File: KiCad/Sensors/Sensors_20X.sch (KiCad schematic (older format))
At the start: 17 parts, among them J1 Conn_02x06_Odd_Even, U1 OPA1641

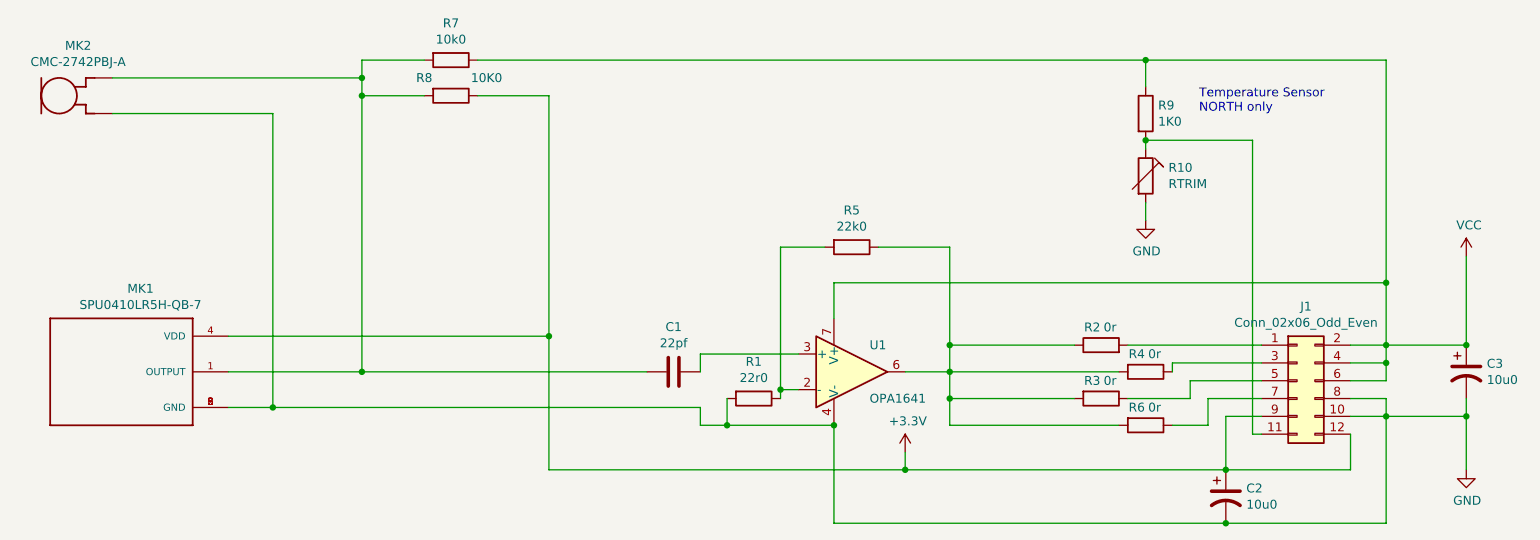
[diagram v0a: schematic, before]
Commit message: Pushing Sensor Revisions
Sensors revised for inverting signal.

Needed since the 'bang' is a negative going wave form that needs to be inverted
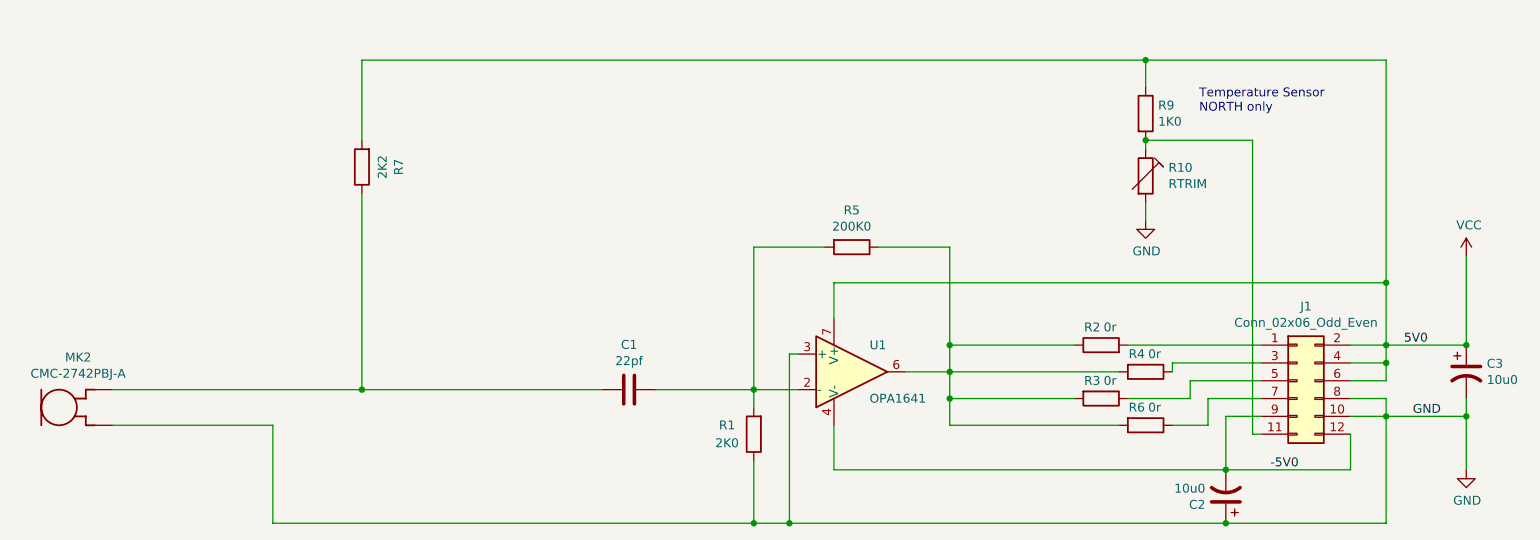
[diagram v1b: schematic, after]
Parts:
- removed MK1: SPU0410LR5H-QB-7, SnapEDA:MIC_SPU0410LR5H-QB-7, symbol SPU0410LR5H-QB-7:SPU0410LR5H-QB-7
- removed R8: 10K0, Resistor_SMD:R_0805_2012Metric, symbol Device:R
- R1: value 22r0 -> 2K0
- R5: value 22k0 -> 200K0
- R7: value 10k0 -> 2K2
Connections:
- net GND: now also C2.1, R1.1, U1.3 (+); no longer C2.2, R1.2, U1.4 (V-)
- net VCC: now also R7.2; no longer R7.1
- net at C1.2, MK2.OUT: now also R7.1; no longer R7.2
- net at R5.2, U1.2 (-): now also C1.1, R1.2; no longer R1.1
- net +3V3 renamed -5V0
- net -5V0: now also C2.2, U1.4 (V-); no longer C2.1
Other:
- moved on the sheet: C1, MK2, R1, R7
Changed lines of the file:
@@
 encoding utf-8
 Sheet 1 1
-Title ""
-Date ""
-Rev ""
+Title "freETarget Sensor Module"
+Date "April 4, 2020"
+Rev "1.0.X"
 Comp ""
-Comment1 ""
+Comment1 "General purpose version for sensor development"
 Comment2 ""
 Comment3 ""
 Comment4 ""
 $EndDescr
-$Comp
-L SPU0410LR5H-QB-7:SPU0410LR5H-QB-7 MK1
-U 1 1 5E68DAEF
-P 2600 4000
-F 0 "MK1" H 2707 4467 50  0000 C CNN
-F 1 "SPU0410LR5H-QB-7" H 2707 4376 50  0000 C CNN
-F 2 "SnapEDA:MIC_SPU0410LR5H-QB-7" H 2600 4000 50  0001 L BNN
-F 3 "Knowles" H 2600 4000 50  0001 L BNN
-F 4 "Manufacturer Recommendations" H 2600 4000 50  0001 L BNN "Field4"
-F 5 "1.2mm" H 2600 4000 50  0001 L BNN "Field5"
-F 6 "H" H 2600 4000 50  0001 L BNN "Field6"
-	1    2600 4000
-	1    0    0    -1
-$EndComp
 $Comp
 L Amplifier_Operational:OPA1641 U1
@@
 $EndComp
 Wire Wire Line
-	6600 4300 6000 4300
-Wire Wire Line
 	7000 4000 7250 4000
 $Comp
 L Device:C C1
 U 1 1 5E6A1DD7
-P 5700 4000
-F 0 "C1" V 5448 4000 50  0000 C CNN
-F 1 "22pf" V 5539 4000 50  0000 C CNN
-F 2 "Resistor_SMD:R_0805_2012Metric" H 5738 3850 50  0001 C CNN
-F 3 "~" H 5700 4000 50  0001 C CNN
-	1    5700 4000
+P 5450 4100
+F 0 "C1" V 5198 4100 50  0000 C CNN
+F 1 "22pf" V 5289 4100 50  0000 C CNN
+F 2 "Resistor_SMD:R_0805_2012Metric" H 5488 3950 50  0001 C CNN
+F 3 "~" H 5450 4100 50  0001 C CNN
+	1    5450 4100
 	0    1    1    0
 $EndComp
@@
 P 6700 3300
 F 0 "R5" V 6493 3300 50  0000 C CNN
-F 1 "22k0" V 6584 3300 50  0000 C CNN
+F 1 "200K0" V 6584 3300 50  0000 C CNN
 F 2 "Resistor_SMD:R_0805_2012Metric" V 6630 3300 50  0001 C CNN
 F 3 "~" H 6700 3300 50  0001 C CNN
@@
 L Device:R R1
 U 1 1 5E6A320A
-P 6150 4150
-F 0 "R1" V 5943 4150 50  0000 C CNN
-F 1 "22r0" V 6034 4150 50  0000 C CNN
-F 2 "Resistor_SMD:R_0805_2012Metric" V 6080 4150 50  0001 C CNN
-F 3 "~" H 6150 4150 50  0001 C CNN
-	1    6150 4150
-	0    1    1    0
-$EndComp
-Wire Wire Line
-	6400 3900 5850 3900
-Wire Wire Line
-	5850 3900 5850 4000
+P 6150 4350
+F 0 "R1" H 6300 4300 50  0000 C CNN
+F 1 "2K0" H 6300 4400 50  0000 C CNN
+F 2 "Resistor_SMD:R_0805_2012Metric" V 6080 4350 50  0001 C CNN
+F 3 "~" H 6150 4350 50  0001 C CNN
+	1    6150 4350
+	-1   0    0    1
+$EndComp
 Wire Wire Line
 	7250 4000 7250 3850
@@
 	7250 3300 6850 3300
 Wire Wire Line
-	6550 3300 6300 3300
-Wire Wire Line
-	6300 3300 6300 4100
-Wire Wire Line
-	6400 4100 6300 4100
-Connection ~ 6300 4100
-Wire Wire Line
-	6300 4100 6300 4150
-Wire Wire Line
-	6000 4150 6000 4300
-Connection ~ 6000 4300
+	6150 3300 6150 4100
 $Comp
 L Device:R R4
@@
 Wire Wire Line
 	9700 4150 9500 4150
-Connection ~ 6600 4300
 Wire Wire Line
 	9500 4250 9700 4250
@@
 F 3 "~" H 8800 4700 50  0001 C CNN
 	1    8800 4700
-	1    0    0    -1
+	-1   0    0    1
 $EndComp
 Wire Wire Line
 	9700 4250 9700 4850
-Wire Wire Line
-	8800 4850 6600 4850
-Wire Wire Line
-	6600 4300 6600 4850
-Connection ~ 8800 4850
 Wire Wire Line
 	10150 4250 9700 4250
@@
 	10150 3850 9700 3850
 Connection ~ 9700 3500
-Wire Wire Line
-	3200 4200 3450 4200
 $Comp
 L Device:R R7
 U 1 1 5E7A9A5C
-P 4450 2250
-F 0 "R7" V 4243 2250 50  0000 C CNN
-F 1 "10k0" V 4334 2250 50  0000 C CNN
-F 2 "Resistor_SMD:R_0805_2012Metric" V 4380 2250 50  0001 C CNN
-F 3 "~" H 4450 2250 50  0001 C CNN
-	1    4450 2250
-	0    1    1    0
+P 3950 2850
+F 0 "R7" V 3743 2850 50  0000 C CNN
+F 1 "2K2" V 3834 2850 50  0000 C CNN
+F 2 "Resistor_SMD:R_0805_2012Metric" V 3880 2850 50  0001 C CNN
+F 3 "~" H 3950 2850 50  0001 C CNN
+	1    3950 2850
+	-1   0    0    1
 $EndComp
 Wire Wire Line
 	9700 2250 9700 3500
-Wire Wire Line
-	4300 2450 3950 2450
-Wire Wire Line
-	3200 4000 3950 4000
-Connection ~ 3450 4200
-Wire Wire Line
-	3950 2450 3950 4000
-Connection ~ 3950 2450
-Connection ~ 3950 4000
-Wire Wire Line
-	3950 4000 5550 4000
-Wire Wire Line
-	5000 2450 5000 3800
-Wire Wire Line
-	3200 3800 5000 3800
-Wire Wire Line
-	4600 2450 5000 2450
-Wire Wire Line
-	4600 2250 8350 2250
-Wire Wire Line
-	5850 4300 5850 4200
-Wire Wire Line
-	3450 4200 5850 4200
-Wire Wire Line
-	5850 4300 6000 4300
-$Comp
-L Device:R R8
-U 1 1 5E7AA2E7
-P 4450 2450
-F 0 "R8" V 4350 2300 50  0000 C CNN
-F 1 "10K0" V 4350 2650 50  0000 C CNN
-F 2 "Resistor_SMD:R_0805_2012Metric" V 4380 2450 50  0001 C CNN
-F 3 "~" H 4450 2450 50  0001 C CNN
-	1    4450 2450
-	0    1    1    0
-$EndComp
-Wire Wire Line
-	3950 2250 4300 2250
 $Comp
 L power:GND #PWR0101
@@
 	10150 4150 10150 4250
 $Comp
-L power:+3.3V #PWR0103
-U 1 1 5E81B6EE
-P 7000 4450
-F 0 "#PWR0103" H 7000 4300 50  0001 C CNN
-F 1 "+3.3V" H 7015 4623 50  0000 C CNN
-F 2 "" H 7000 4450 50  0001 C CNN
-F 3 "" H 7000 4450 50  0001 C CNN
-	1    7000 4450
-	1    0    0    -1
-$EndComp
-Wire Wire Line
-	7000 4450 7000 4550
-Wire Wire Line
-	3450 2550 3450 4200
-$Comp
 L CMC-2742PBJ-A:CMC-2742PBJ-A MK2
 U 1 1 5E7C8206
-P 2250 2450
-F 0 "MK2" H 2357 2731 50  0000 C CNN
-F 1 "CMC-2742PBJ-A" H 2357 2640 50  0000 C CNN
-F 2 "CUI_CMC-2742PBJ-A" H 2250 2450 50  0001 L BNN
-F 3 "CUI INC" H 2250 2450 50  0001 L BNN
-F 4 "Manufacturer recommendations" H 2250 2450 50  0001 L BNN "Field4"
-	1    2250 2450
+P 2250 4200
+F 0 "MK2" H 2357 4481 50  0000 C CNN
+F 1 "CMC-2742PBJ-A" H 2357 4390 50  0000 C CNN
+F 2 "CUI_CMC-2742PBJ-A" H 2250 4200 50  0001 L BNN
+F 3 "CUI INC" H 2250 4200 50  0001 L BNN
+F 4 "Manufacturer recommendations" H 2250 4200 50  0001 L BNN "Field4"
+	1    2250 4200
 	1    0    0    -1
 $EndComp
@@
 $EndComp
 Wire Wire Line
-	7000 4550 8800 4550
-Wire Wire Line
 	8800 4550 9500 4550
-Wire Wire Line
-	8800 4850 9700 4850
 Wire Wire Line
 	9000 4250 8800 4250
@@
 Temperature Sensor\nNORTH only
 Wire Wire Line
-	3950 2250 3950 2350
-Wire Wire Line
-	2550 2550 3450 2550
-Wire Wire Line
-	2550 2350 3950 2350
-Connection ~ 3950 2350
-Wire Wire Line
-	3950 2350 3950 2450
-Wire Wire Line
-	7000 4550 5000 4550
-Wire Wire Line
-	5000 4550 5000 3800
-Connection ~ 7000 4550
-Connection ~ 5000 3800
+	2550 4300 3450 4300
+Wire Wire Line
+	8800 4850 9700 4850
+Wire Wire Line
+	8800 4550 6600 4550
+Wire Wire Line
+	6600 4550 6600 4300
+Text Label 9050 4550 0    50   ~ 0
+-5V0
+Connection ~ 6150 4100
+Wire Wire Line
+	6150 4200 6150 4100
+Wire Wire Line
+	6150 4500 6150 4850
+Wire Wire Line
+	5600 4100 6150 4100
+Wire Wire Line
+	6150 4100 6400 4100
+Wire Wire Line
+	3950 4100 5300 4100
+Wire Wire Line
+	3450 4850 6150 4850
+Connection ~ 6150 4850
+Wire Wire Line
+	6150 4850 6350 4850
+Connection ~ 8800 4850
+Wire Wire Line
+	6150 3300 6550 3300
+Wire Wire Line
+	6400 3900 6350 3900
+Wire Wire Line
+	6350 3900 6350 4850
+Connection ~ 6350 4850
+Wire Wire Line
+	6350 4850 8800 4850
+Text Label 9850 4250 0    50   ~ 0
+GND
+Text Label 9800 3850 0    50   ~ 0
+5V0
+Wire Wire Line
+	3950 3000 3950 4100
+Wire Wire Line
+	3950 2250 3950 2700
+Wire Wire Line
+	3950 2250 8350 2250
+Wire Wire Line
+	3450 4300 3450 4850
+Wire Wire Line
+	2550 4100 3950 4100
+Connection ~ 3950 4100
 $EndSCHEMATC
